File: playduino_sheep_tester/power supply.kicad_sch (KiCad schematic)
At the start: 32 parts, among them J1 Conn_01x02_Socket, K1 G6K-2F-Y-TR DC5, Q1 IRF7416PbF, Q10 E18P100KC, Q5 E18P100KC, Q6 E18P100KC, Q7 BSS123, Q8 AO3416, Q9 BSS123, U10 B0524S-2WR3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

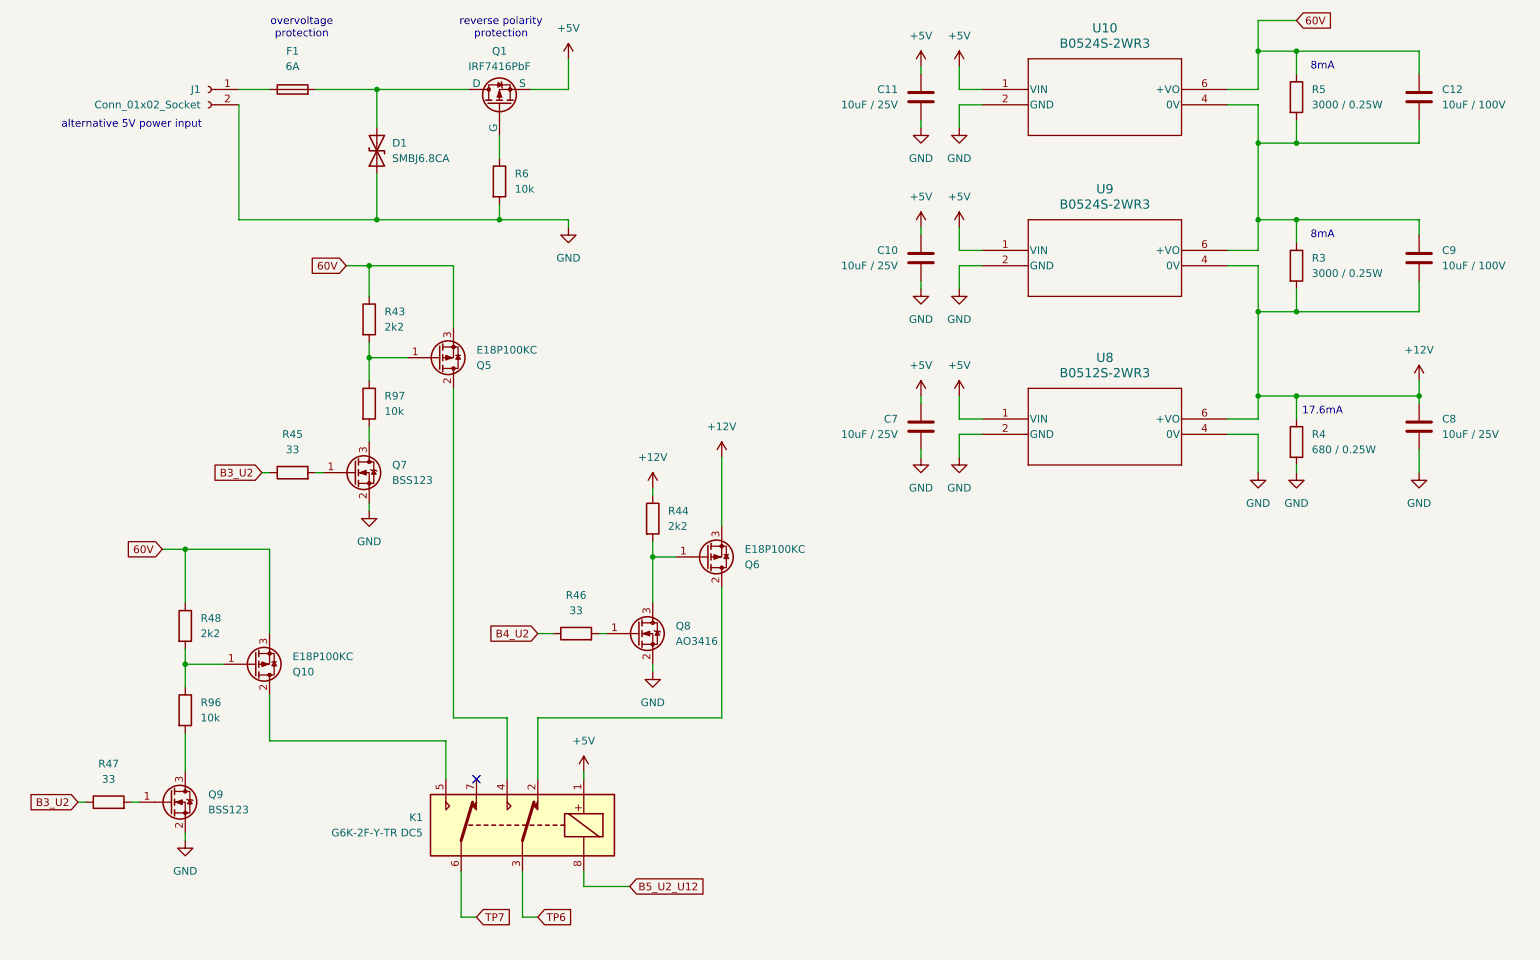
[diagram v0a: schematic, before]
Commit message: small improvements and fixing horrible mistakes
change A3_U2 and B7_U2 because of known issues with MCP23017
https://support.microchip.com/s/article/GPA7---GPB7-Cannot-Be-Used-as-Inputs-In-MCP23017

add resistor to MCP23017 address pins

replace B3_U2 duplicate with B6_U3
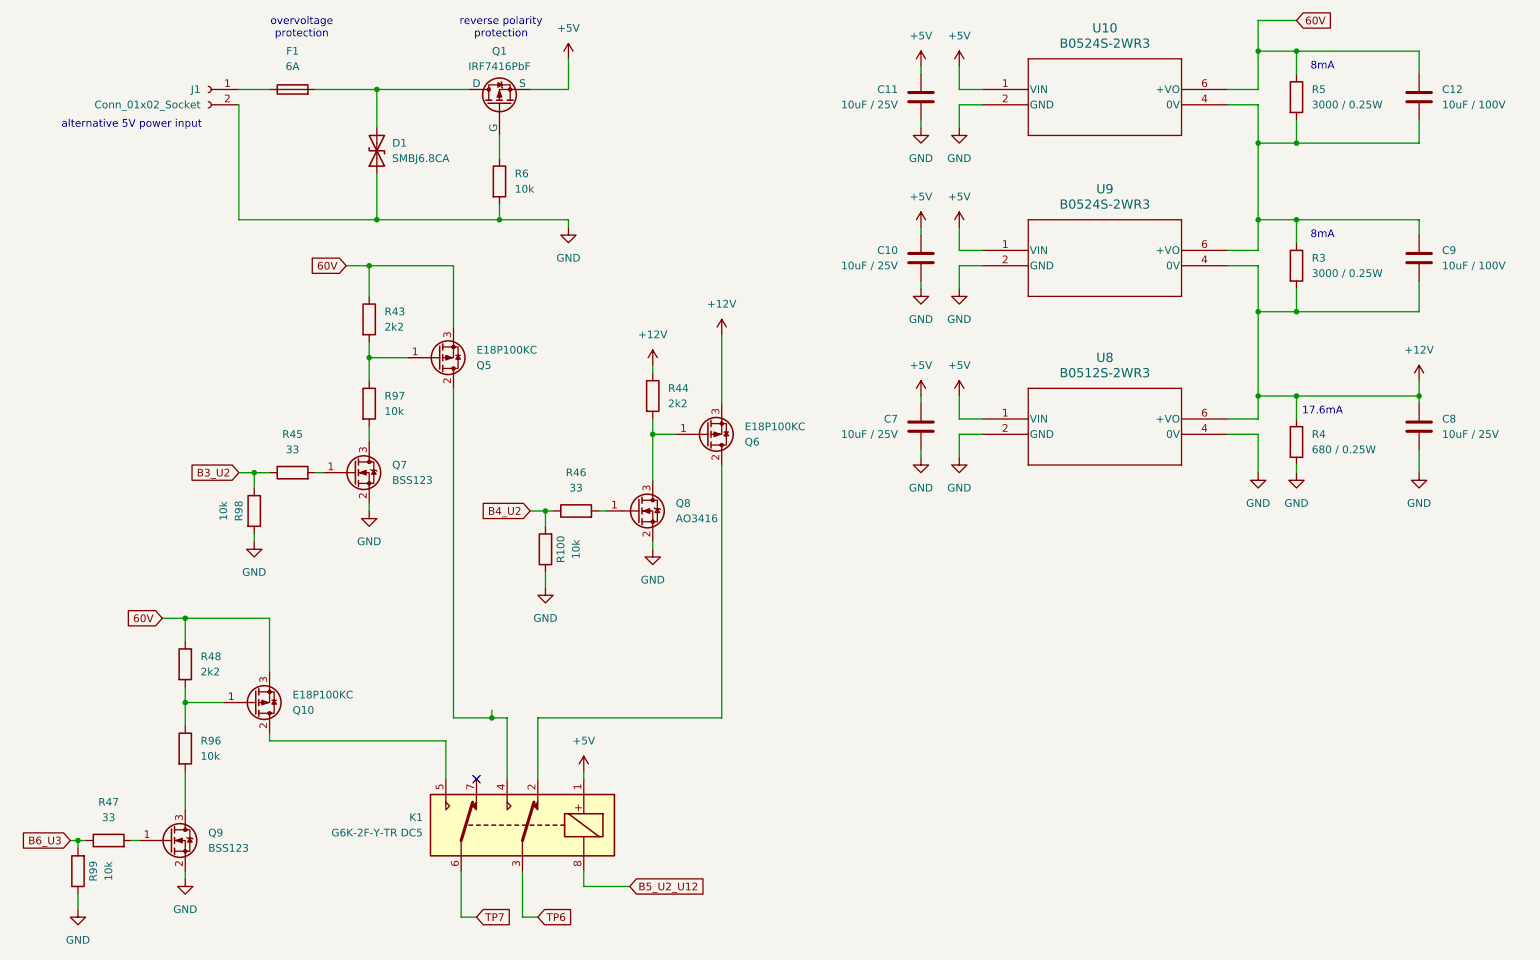
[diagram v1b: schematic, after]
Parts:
- added R100, R98, R99: 10k, Resistor_SMD:R_0603_1608Metric, symbol Device:R
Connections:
- net B3_U2: now also R98.1; no longer R47.1
- net B4_U2: now also R100.2
- net GND: now also R100.1, R98.2, R99.1
- new net B6_U3: R47.1, R99.2
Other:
- moved on the sheet: Q10, Q6, Q8, Q9, R44, R46, R47, R48, R96
